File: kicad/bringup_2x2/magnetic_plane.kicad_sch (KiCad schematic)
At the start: 14 parts

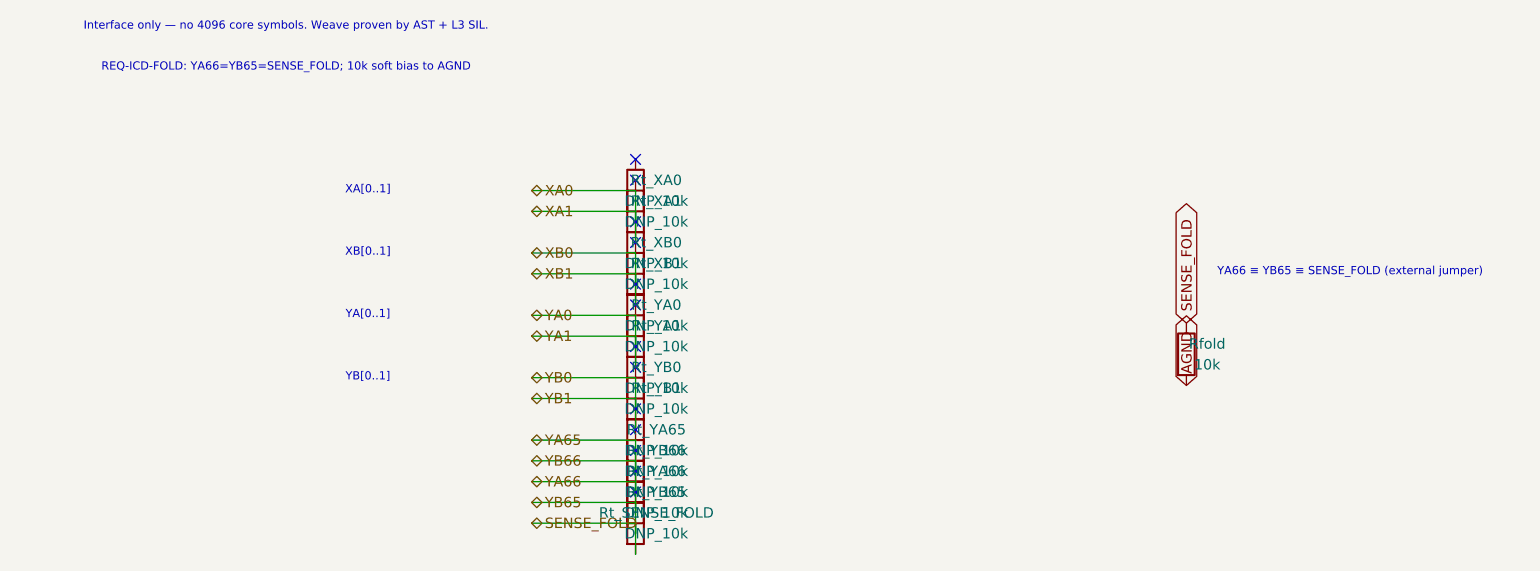
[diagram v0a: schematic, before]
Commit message: logical seperation into host and multiple decode/drive/steering boards
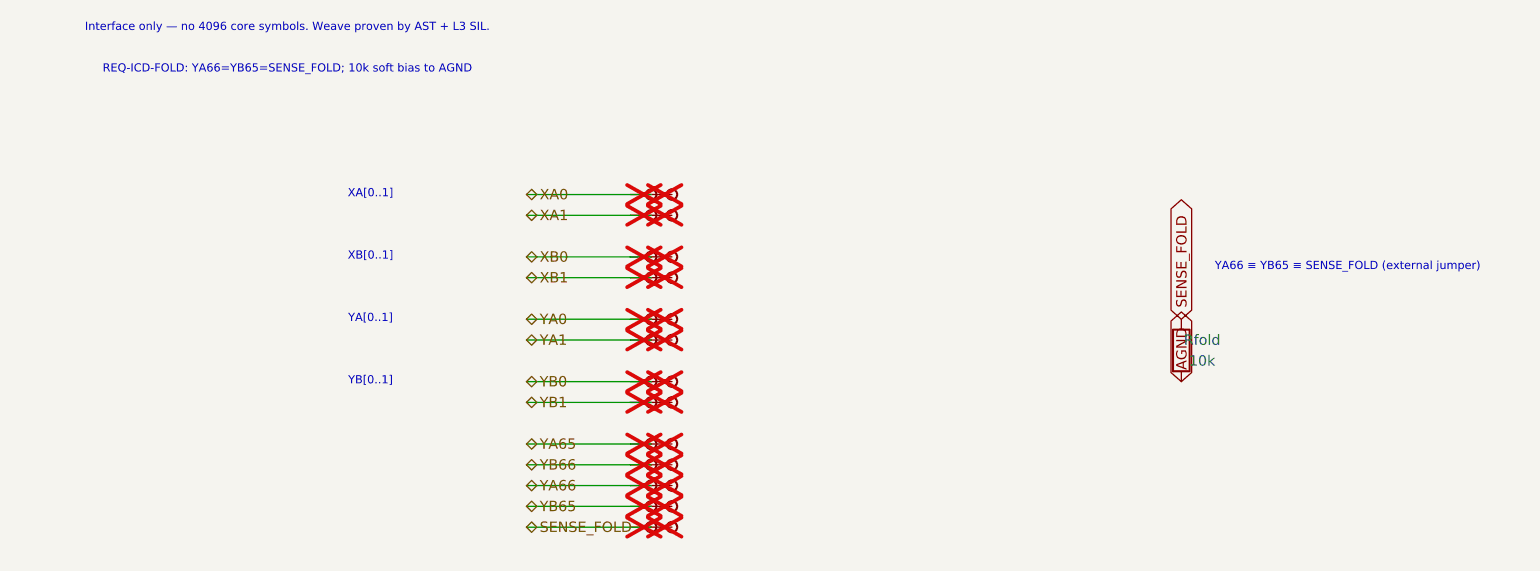
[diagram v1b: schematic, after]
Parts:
- removed Rt_SENSE_FOLD, Rt_XA0, Rt_XA1, Rt_XB0, Rt_XB1, Rt_YA0, Rt_YA1, Rt_YA65, Rt_YA66, Rt_YB0, Rt_YB1, Rt_YB65, Rt_YB66: DNP_10k, symbol Device:R
- added TP_SENSE_FOLD, TP_SENSE_FOLDb, TP_XA0, TP_XA0b, TP_XA1, TP_XA1b, TP_XB0, TP_XB0b, TP_XB1, TP_XB1b, TP_YA0, TP_YA0b, TP_YA1, TP_YA1b, TP_YA65, TP_YA65b, TP_YA66, TP_YA66b, TP_YB0, TP_YB0b, TP_YB1, TP_YB1b, TP_YB65, TP_YB65b, TP_YB66, TP_YB66b: Stub, symbol CMR:Stub
- Rfold: symbol Device:R -> CMR:R
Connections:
- net SENSE_FOLD: now also TP_SENSE_FOLD.1, TP_SENSE_FOLDb.1
- net XA0: now also TP_XA0.1, TP_XA0b.1
- net XB0: now also TP_XB0.1, TP_XB0b.1
- net YA0: now also TP_YA0.1, TP_YA0b.1
- net YB0: now also TP_YB0.1, TP_YB0b.1
- new net XA1: TP_XA1.1, TP_XA1b.1
- new net XB1: TP_XB1.1, TP_XB1b.1
- new net YA1: TP_YA1.1, TP_YA1b.1
- new net YA65: TP_YA65.1, TP_YA65b.1
- new net YA66: TP_YA66.1, TP_YA66b.1
- new net YB1: TP_YB1.1, TP_YB1b.1
- new net YB65: TP_YB65.1, TP_YB65b.1
- new net YB66: TP_YB66.1, TP_YB66b.1
- no-connect marks 13 -> 0
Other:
- moved on the sheet: Rfold
